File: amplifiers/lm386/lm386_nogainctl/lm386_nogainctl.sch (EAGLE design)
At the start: 12 parts, among them IC1 LM386N-4

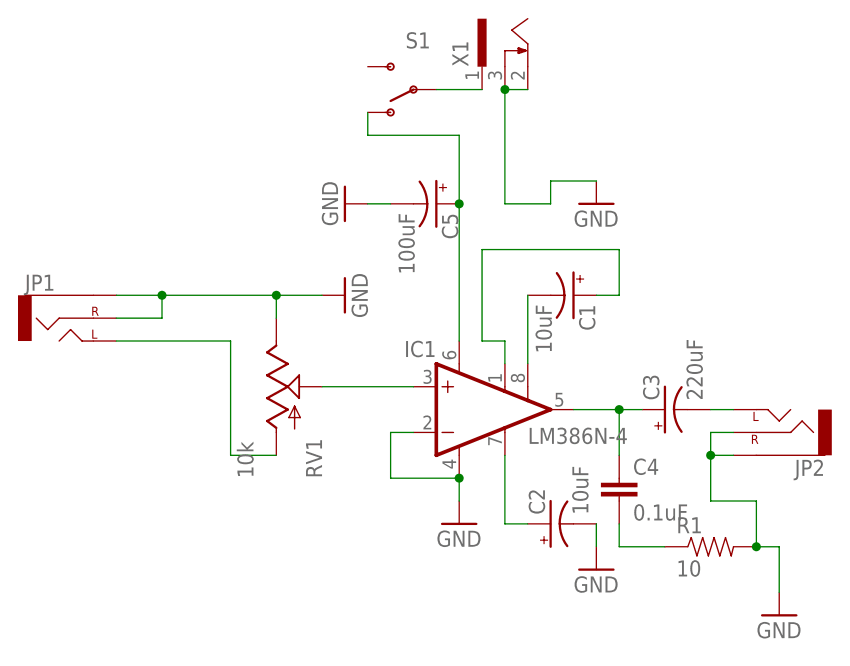
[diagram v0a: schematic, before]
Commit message: updated to version 3, check on screw size and hole placement needed for confirmation
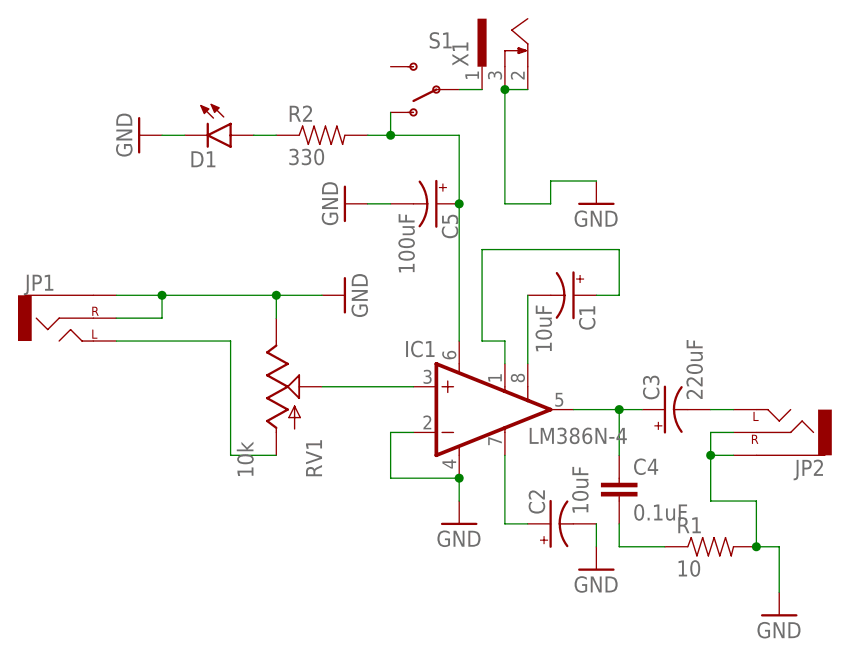
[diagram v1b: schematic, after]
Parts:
- added D1: (no value), SparkFun-LED:LED3MM
- added R2: 330, SparkFun-Resistors:RESISTORPTH-1/4W
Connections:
- new net N$10: D1.A, R2.1
- net GND: now also D1.C
- net N$4: now also R2.2
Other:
- moved on the sheet: S1
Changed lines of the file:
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@@
 <grid distance="0.1" unitdist="inch" unit="inch" style="lines" multiple="1" display="no" altdistance="0.01" altunitdist="inch" altunit="inch"/>
 <layers>
-<layer number="1" name="Top" color="4" fill="1" visible="yes" active="no"/>
-<layer number="16" name="Bottom" color="1" fill="1" visible="yes" active="no"/>
-<layer number="17" name="Pads" color="2" fill="1" visible="yes" active="no"/>
-<layer number="18" name="Vias" color="2" fill="1" visible="yes" active="no"/>
-<layer number="19" name="Unrouted" color="6" fill="1" visible="yes" active="no"/>
-<layer number="20" name="Dimension" color="15" fill="1" visible="yes" active="no"/>
-<layer number="21" name="tPlace" color="7" fill="1" visible="yes" active="no"/>
-<layer number="22" name="bPlace" color="7" fill="1" visible="yes" active="no"/>
-<layer number="23" name="tOrigins" color="15" fill="1" visible="yes" active="no"/>
-<layer number="24" name="bOrigins" color="15" fill="1" visible="yes" active="no"/>
-<layer number="25" name="tNames" color="7" fill="1" visible="yes" active="no"/>
-<layer number="26" name="bNames" color="7" fill="1" visible="yes" active="no"/>
-<layer number="27" name="tValues" color="7" fill="1" visible="yes" active="no"/>
-<layer number="28" name="bValues" color="7" fill="1" visible="yes" active="no"/>
+<layer number="1" name="Top" color="4" fill="1" visible="no" active="no"/>
+<layer number="16" name="Bottom" color="1" fill="1" visible="no" active="no"/>
+<layer number="17" name="Pads" color="2" fill="1" visible="no" active="no"/>
+<layer number="18" name="Vias" color="2" fill="1" visible="no" active="no"/>
+<layer number="19" name="Unrouted" color="6" fill="1" visible="no" active="no"/>
+<layer number="20" name="Dimension" color="15" fill="1" visible="no" active="no"/>
+<layer number="21" name="tPlace" color="7" fill="1" visible="no" active="no"/>
+<layer number="22" name="bPlace" color="7" fill="1" visible="no" active="no"/>
+<layer number="23" name="tOrigins" color="15" fill="1" visible="no" active="no"/>
+<layer number="24" name="bOrigins" color="15" fill="1" visible="no" active="no"/>
+<layer number="25" name="tNames" color="7" fill="1" visible="no" active="no"/>
+<layer number="26" name="bNames" color="7" fill="1" visible="no" active="no"/>
+<layer number="27" name="tValues" color="7" fill="1" visible="no" active="no"/>
+<layer number="28" name="bValues" color="7" fill="1" visible="no" active="no"/>
 <layer number="29" name="tStop" color="7" fill="3" visible="no" active="no"/>
 <layer number="30" name="bStop" color="7" fill="6" visible="no" active="no"/>
@@
 <layer number="35" name="tGlue" color="7" fill="4" visible="no" active="no"/>
 <layer number="36" name="bGlue" color="7" fill="5" visible="no" active="no"/>
-<layer number="37" name="tTest" color="7" fill="1" visible="yes" active="no"/>
-<layer number="38" name="bTest" color="7" fill="1" visible="yes" active="no"/>
+<layer number="37" name="tTest" color="7" fill="1" visible="no" active="no"/>
+<layer number="38" name="bTest" color="7" fill="1" visible="no" active="no"/>
 <layer number="39" name="tKeepout" color="4" fill="11" visible="no" active="no"/>
 <layer number="40" name="bKeepout" color="1" fill="11" visible="no" active="no"/>
@@
 <layer number="44" name="Drills" color="7" fill="1" visible="no" active="no"/>
 <layer number="45" name="Holes" color="7" fill="1" visible="no" active="no"/>
-<layer number="46" name="Milling" color="3" fill="1" visible="yes" active="no"/>
-<layer number="47" name="Measures" color="7" fill="1" visible="yes" active="no"/>
-<layer number="48" name="Document" color="7" fill="1" visible="yes" active="no"/>
-<layer number="49" name="Reference" color="7" fill="1" visible="yes" active="no"/>
-<layer number="50" name="dxf" color="7" fill="1" visible="yes" active="no"/>
-<layer number="51" name="tDocu" color="7" fill="1" visible="yes" active="no"/>
-<layer number="52" name="bDocu" color="7" fill="1" visible="yes" active="no"/>
-<layer number="53" name="tGND_GNDA" color="7" fill="9" visible="yes" active="no"/>
-<layer number="54" name="bGND_GNDA" color="1" fill="9" visible="yes" active="no"/>
-<layer number="56" name="wert" color="7" fill="1" visible="yes" active="no"/>
-<layer number="57" name="tCAD" color="7" fill="1" visible="yes" active="no"/>
-<layer number="59" name="tCarbon" color="7" fill="1" visible="yes" active="no"/>
-<layer number="60" name="bCarbon" color="7" fill="1" visible="yes" active="no"/>
+<layer number="46" name="Milling" color="3" fill="1" visible="no" active="no"/>
+<layer number="47" name="Measures" color="7" fill="1" visible="no" active="no"/>
+<layer number="48" name="Document" color="7" fill="1" visible="no" active="no"/>
+<layer number="49" name="Reference" color="7" fill="1" visible="no" active="no"/>
+<layer number="50" name="dxf" color="7" fill="1" visible="no" active="no"/>
+<layer number="51" name="tDocu" color="7" fill="1" visible="no" active="no"/>
+<layer number="52" name="bDocu" color="7" fill="1" visible="no" active="no"/>
+<layer number="53" name="tGND_GNDA" color="7" fill="9" visible="no" active="no"/>
+<layer number="54" name="bGND_GNDA" color="1" fill="9" visible="no" active="no"/>
+<layer number="56" name="wert" color="7" fill="1" visible="no" active="no"/>
+<layer number="57" name="tCAD" color="7" fill="1" visible="no" active="no"/>
+<layer number="59" name="tCarbon" color="7" fill="1" visible="no" active="no"/>
+<layer number="60" name="bCarbon" color="7" fill="1" visible="no" active="no"/>
 <layer number="90" name="Modules" color="5" fill="1" visible="yes" active="yes"/>
 <layer number="91" name="Nets" color="2" fill="1" visible="yes" active="yes"/>
@@
 <part name="C4" library="SparkFun-Capacitors" deviceset="CAP" device="PTH2" value="0.1uF"/>
 <part name="X1" library="con-shiua-chyuan" deviceset="SCD-014A" device=""/>
+<part name="D1" library="SparkFun-LED" deviceset="LED" device="3MM"/>
+<part name="R2" library="SparkFun-Resistors" deviceset="RESISTOR" device="PTH-1/4W" value="330"/>
+<part name="GND7" library="SparkFun-Aesthetics" deviceset="GND" device=""/>
 </parts>
 <sheets>
@@
 <instance part="C5" gate="G$1" x="68.58" y="68.58" rot="R270"/>
 <instance part="GND6" gate="1" x="58.42" y="68.58" rot="R270"/>
-<instance part="S1" gate="1" x="66.04" y="81.28" rot="R180"/>
+<instance part="S1" gate="1" x="68.58" y="81.28" rot="R180"/>
 <instance part="C4" gate="G$1" x="88.9" y="35.56"/>
 <instance part="X1" gate="G$1" x="76.2" y="86.36" rot="R90"/>
+<instance part="D1" gate="G$1" x="45.72" y="76.2" rot="R270"/>
+<instance part="R2" gate="G$1" x="55.88" y="76.2"/>
+<instance part="GND7" gate="1" x="35.56" y="76.2" rot="R270"/>
 </instances>
 <busses>
@@
 <junction x="76.2" y="81.28"/>
 </segment>
+<segment>
+<pinref part="GND7" gate="1" pin="GND"/>
+<pinref part="D1" gate="G$1" pin="C"/>
+<wire x1="38.1" y1="76.2" x2="40.64" y2="76.2" width="0.1524" layer="91"/>
+</segment>
 </net>
 <net name="N$4" class="0">
 <segment>
 <pinref part="S1" gate="1" pin="O"/>
-<wire x1="60.96" y1="78.74" x2="60.96" y2="76.2" width="0.1524" layer="91"/>
+<wire x1="63.5" y1="78.74" x2="63.5" y2="76.2" width="0.1524" layer="91"/>
 <pinref part="IC1" gate="G$1" pin="VS"/>
 <pinref part="C5" gate="G$1" pin="+"/>
 <wire x1="71.12" y1="68.58" x2="71.12" y2="53.34" width="0.1524" layer="91"/>
-<wire x1="60.96" y1="76.2" x2="71.12" y2="76.2" width="0.1524" layer="91"/>
+<wire x1="63.5" y1="76.2" x2="71.12" y2="76.2" width="0.1524" layer="91"/>
 <wire x1="71.12" y1="76.2" x2="71.12" y2="68.58" width="0.1524" layer="91"/>
 <junction x="71.12" y="68.58"/>
+<pinref part="R2" gate="G$1" pin="2"/>
+<wire x1="60.96" y1="76.2" x2="63.5" y2="76.2" width="0.1524" layer="91"/>
+<junction x="63.5" y="76.2"/>
 </segment>
 </net>
@@
 <pinref part="S1" gate="1" pin="P"/>
 <pinref part="X1" gate="G$1" pin="1"/>
-<wire x1="68.58" y1="81.28" x2="73.66" y2="81.28" width="0.1524" layer="91"/>
-</segment>
-</net>
+<wire x1="71.12" y1="81.28" x2="73.66" y2="81.28" width="0.1524" layer="91"/>
+</segment>
+</net>
+<net name="N$10" class="0">
+<segment>
+<pinref part="D1" gate="G$1" pin="A"/>
+<pinref part="R2" gate="G$1" pin="1"/>
+<wire x1="48.26" y1="76.2" x2="50.8" y2="76.2" width="0.1524" layer="91"/>
+</segment>
+</net>
